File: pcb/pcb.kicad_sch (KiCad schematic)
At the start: 5 parts, among them J1 AudioJack3, J2 Conn_01x07, J3 Conn_01x07, U1 SeeeduinoXIAO

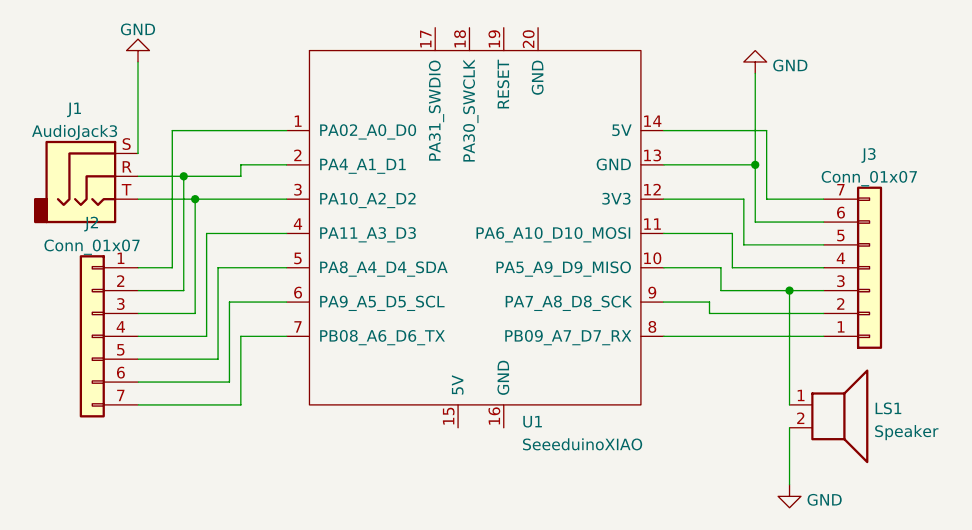
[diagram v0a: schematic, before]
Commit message: Route buzzer to XIAO pin 10, not 9. New KiCAD.
Fixes #5
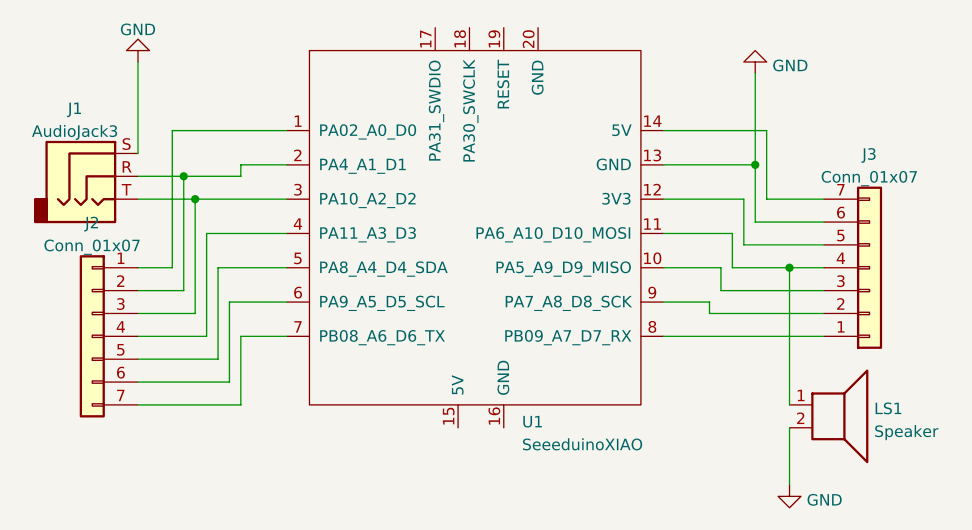
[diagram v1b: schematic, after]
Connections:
- net at J3.3 (Pin_3), U1.10 (PA5_A9_D9_MISO): no longer LS1.1
- net at J3.4 (Pin_4), U1.11 (PA6_A10_D10_MOSI): now also LS1.1
